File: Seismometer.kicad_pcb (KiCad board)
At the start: 4 copper layers, 91 parts, among them J4 Conn_01x03_Socket, J5 Conn_01x03_Socket, J6 Conn_01x03_Socket, U1 DLVR-F50D, U2 MC3479, U3 ADS131M04-Q1, U4 LP5907MFX-3.3, U5 Teensy4.1, X1 ASE-xxxMHz

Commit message: Initial layout complete
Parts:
- moved R22 55.8 mm to (156.7, 150.9)
- moved R1 43.9 mm to (131.5, 135.6), turned to 180 degrees
- moved R2 43.6 mm to (131.5, 133.1), turned to 180 degrees
- moved R48 29.5 mm to (175.3, 153.9)
- moved C12 29.5 mm to (175.3, 151.6)
- moved C14 29.5 mm to (180.8, 149.4)
- moved FB2 29.5 mm to (175.3, 149.4)
- moved U4 29.5 mm to (180.9, 153.0)
- moved R25 29.3 mm to (156.5, 115.3)
- moved R6 25.4 mm to (156.7, 105.2)
- moved C5 22.6 mm to (106.4, 116.9), turned to -90 degrees
- moved C6 22.2 mm to (108.5, 116.8), turned to -90 degrees
- moved R3 21.6 mm to (177.8, 135.9)
- moved R39 19.7 mm to (181.4, 135.9), turned to 0 degrees
- moved C1 18.8 mm to (166.8, 124.0)
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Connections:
- C3 pad 1: /3V3_TEENSY -> Net-(C3-Pad1)
- C4 pad 1: /3V3_TEENSY -> GND
- C4 pad 2: GND -> Net-(C4-Pad2)
- R21 pad 1: GND -> /~{CS_ACCEL}
- R22 pad 2: Net-(U5-32_OUT1B) -> Net-(U5-0_RX1_CRX2_CS1)
- R25 pad 1: Net-(U5-35_TX8) -> GND
- R25 pad 2: GND -> Net-(U5-24_A10_TX6_SCL2)
- R46 pad 2: Net-(U5-24_A10_TX6_SCL2) -> /ADC_DRDY
- R47 pad 2: Net-(U5-28_RX7) -> /ADC_SYNC/RESET
- R5 pad 2: /~{CS_ACCEL} -> /~{CS_ADC}
- R6 pad 1: Net-(U5-36_CS) -> GND
- R6 pad 2: /~{CS_ADC} -> Net-(U5-28_RX7)
- U5 pad 15: /3V3_TEENSY -> Net-(C4-Pad2)
- U5 pad 2: /INT_ACCEL -> Net-(U5-0_RX1_CRX2_CS1)
- U5 pad 24: Net-(U5-32_OUT1B) -> /INT_ACCEL
- U5 pad 27: Net-(U5-35_TX8) -> /ADC_DRDY
- U5 pad 28: Net-(U5-36_CS) -> /ADC_SYNC/RESET
- U5 pad 46: /3V3_TEENSY -> Net-(C3-Pad1)
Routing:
- net /SCK: track 0.00 -> 103.9 mm, vias 0 -> 3
- net /MOSI: track 0.00 -> 94.8 mm, vias 0 -> 2
- net /MISO: track 0.00 -> 86.1 mm, vias 0 -> 2
- net /SDA: track 0.00 -> 42.3 mm
- net /SCL: track 0.00 -> 42.3 mm
- net /Geophone Z/V-: track 2.24 -> 43.8 mm
- net Net-(U5-VIN): track 6.36 -> 47.5 mm
- net /Geophone Z/V+: track 2.35 -> 42.0 mm
- net /Geophone Y/V+: track 2.35 -> 38.4 mm
- net /INT_DLVR: track 1.80 -> 34.7 mm
- net /Geophone Y/V-: track 2.24 -> 31.4 mm
- net /INT_ACCEL: track 0.00 -> 21.9 mm
- net /ADC_DRDY: track 0.00 -> 21.3 mm
- net /~{CS_ADC}: track 0.00 -> 19.0 mm
- net /ADC_SYNC/RESET: track 0.00 -> 18.2 mm
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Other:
- board outline added: 92.7 x 65 mm

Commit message: Ready
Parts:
- added REF**: MountingHole_3.2mm_M3_DIN965, MountingHole:MountingHole_3.2mm_M3_DIN965, F.Cu at (119.6, 125.2)
- added REF**: MountingHole_3.2mm_M3_DIN965, MountingHole:MountingHole_3.2mm_M3_DIN965, F.Cu at (180.2, 79.8)
- added REF**: MountingHole_3.2mm_M3_DIN965, MountingHole:MountingHole_3.2mm_M3_DIN965, F.Cu at (97.5, 69.2)
- added REF**: MountingHole_3.2mm_M3_DIN965, MountingHole:MountingHole_3.2mm_M3_DIN965, F.Cu at (180.2, 115.6)
- X1: value ASE-xxxMHz -> SIT8924BA-22-33E-8.192000G
- moved C18 26.3 mm to (113.9, 123.6)
- moved R37 26.3 mm to (130.0, 117.0)
- moved R52 26.3 mm to (108.0, 103.5)
- moved R8 26.3 mm to (155.2, 117.0)
- moved C1 26.3 mm to (165.3, 97.7)
- moved C10 26.3 mm to (105.6, 76.7)
- moved C11 26.3 mm to (111.7, 72.9)
- moved C12 26.3 mm to (173.8, 125.3)
- moved C13 26.3 mm to (111.7, 68.8)
- moved C14 26.3 mm to (179.3, 123.1)
- moved C15 26.3 mm to (130.0, 127.2)
- moved C2 26.3 mm to (130.0, 124.9)
- moved C3 26.3 mm to (130.0, 122.1)
- moved C4 26.3 mm to (155.2, 91.6)
- moved C5 26.3 mm to (105.0, 90.7)
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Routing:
- net /MISO: track 86.1 -> 87.2 mm, vias 2 -> 0
- net GND: track 9.66 -> 10.0 mm, vias 68 -> 67
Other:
- board text added: "1 TOP"
- board text added: "2 GND"
- board text added: "3 PWR"
- board text added: "4 BOTTOM"
- board text added: "Seismometer V0.1"
- board text added: "Sytse Reitsma"

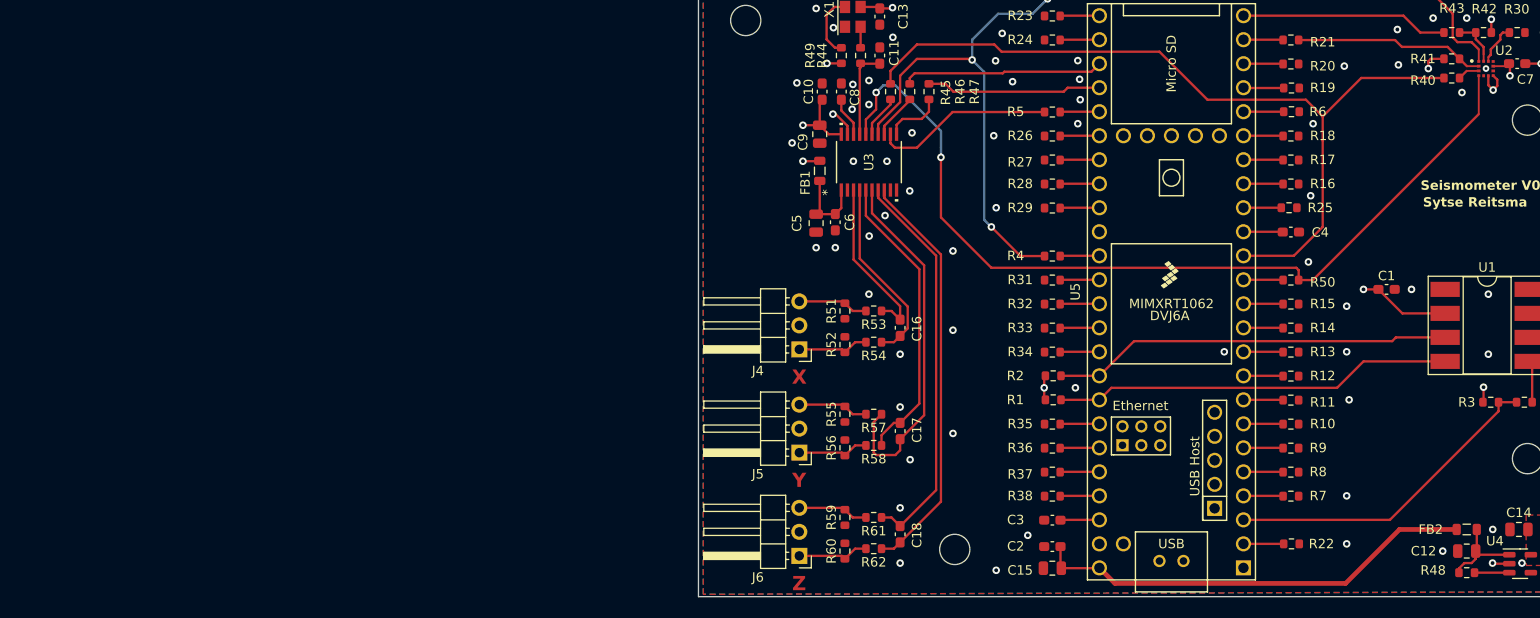
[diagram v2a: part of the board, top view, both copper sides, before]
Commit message: Active input filter
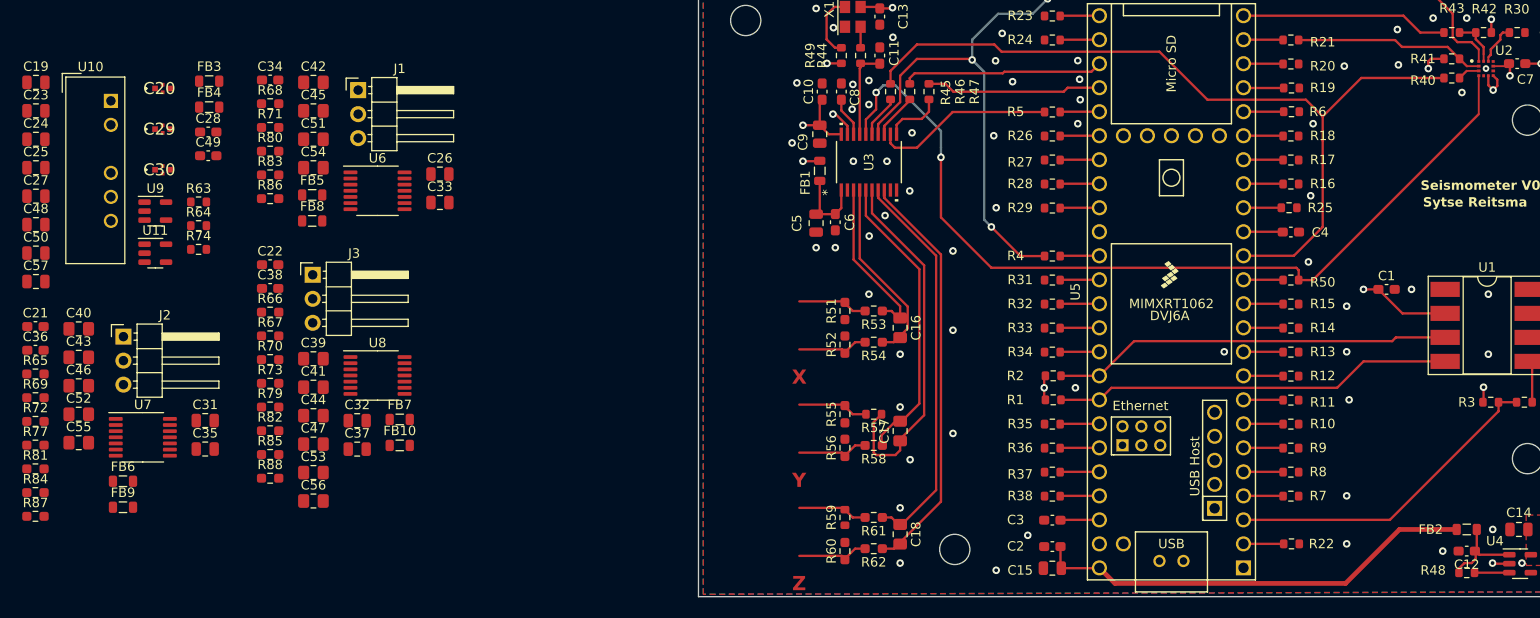
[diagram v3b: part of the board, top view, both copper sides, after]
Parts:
- removed J4, J5, J6: Conn_01x03_Socket, Connector_PinHeader_2.54mm:PinHeader_1x03_P2.54mm_Horizontal
- added C19: 2.2u, Capacitor_SMD:C_0805_2012Metric, F.Cu at (22.4, 75.8)
- added C20: NFM18PC104R1C3D, seismometer:NFM18PC104R1C3D, F.Cu at (35.8, 76.4)
- added C21: 100n, Capacitor_SMD:C_0603_1608Metric_Pad1.08x0.95mm_HandSolder, F.Cu at (22.4, 101.6)
- added C22: 100n, Capacitor_SMD:C_0603_1608Metric_Pad1.08x0.95mm_HandSolder, F.Cu at (47.2, 95.1)
- added C23: 100n, Capacitor_SMD:C_0805_2012Metric, F.Cu at (22.4, 78.8)
- added C24: 2.2u, Capacitor_SMD:C_0805_2012Metric, F.Cu at (22.4, 81.8)
- added C25: 2.2u, Capacitor_SMD:C_0805_2012Metric, F.Cu at (22.4, 84.8)
- added C26: 2.2u, Capacitor_SMD:C_0805_2012Metric, F.Cu at (65.2, 85.5)
- added C27: 2.2u, Capacitor_SMD:C_0805_2012Metric, F.Cu at (22.4, 87.8)
- added C28: 100n, Capacitor_SMD:C_0603_1608Metric_Pad1.08x0.95mm_HandSolder, F.Cu at (40.7, 81.0)
- added C29: NFM18PC104R1C3D, seismometer:NFM18PC104R1C3D, F.Cu at (35.8, 80.7)
- added C30: NFM18PC104R1C3D, seismometer:NFM18PC104R1C3D, F.Cu at (35.8, 85.0)
- added C31: 2.2u, Capacitor_SMD:C_0805_2012Metric, F.Cu at (40.3, 111.5)
- added C32: 2.2u, Capacitor_SMD:C_0805_2012Metric, F.Cu at (56.4, 111.6)
- added C33: 2.2u, Capacitor_SMD:C_0805_2012Metric, F.Cu at (65.2, 88.5)
- added C34: 100n, Capacitor_SMD:C_0603_1608Metric_Pad1.08x0.95mm_HandSolder, F.Cu at (47.2, 75.5)
- added C35: 2.2u, Capacitor_SMD:C_0805_2012Metric, F.Cu at (40.3, 114.6)
- added C36: 100n, Capacitor_SMD:C_0603_1608Metric_Pad1.08x0.95mm_HandSolder, F.Cu at (22.4, 104.1)
- added C37: 2.2u, Capacitor_SMD:C_0805_2012Metric, F.Cu at (56.4, 114.6)
- added C38: 100n, Capacitor_SMD:C_0603_1608Metric_Pad1.08x0.95mm_HandSolder, F.Cu at (47.2, 97.6)
- added C39: 1.6u X7R, Capacitor_SMD:C_0805_2012Metric_Pad1.18x1.45mm_HandSolder, F.Cu at (51.8, 105.0)
- added C40: 10u X7R, Capacitor_SMD:C_0805_2012Metric_Pad1.18x1.45mm_HandSolder, F.Cu at (27.0, 101.8)
- added C41: 10u X7R, Capacitor_SMD:C_0805_2012Metric_Pad1.18x1.45mm_HandSolder, F.Cu at (51.8, 108.0)
- added C42: 360n X7R, Capacitor_SMD:C_0805_2012Metric_Pad1.18x1.45mm_HandSolder, F.Cu at (51.8, 75.8)
- added C43: 360n X7R, Capacitor_SMD:C_0805_2012Metric_Pad1.18x1.45mm_HandSolder, F.Cu at (27.0, 104.9)
- added C44: 360n X7R, Capacitor_SMD:C_0805_2012Metric_Pad1.18x1.45mm_HandSolder, F.Cu at (51.8, 111.0)
- added C45: 1.6u X7R, Capacitor_SMD:C_0805_2012Metric_Pad1.18x1.45mm_HandSolder, F.Cu at (51.8, 78.8)
- added C46: 1.6u X7R, Capacitor_SMD:C_0805_2012Metric_Pad1.18x1.45mm_HandSolder, F.Cu at (27.0, 107.9)
- added C47: 1.6u X7R, Capacitor_SMD:C_0805_2012Metric_Pad1.18x1.45mm_HandSolder, F.Cu at (51.8, 114.0)
- added C48: 2.2u, Capacitor_SMD:C_0805_2012Metric, F.Cu at (22.4, 90.8)
- added C49: 100n, Capacitor_SMD:C_0603_1608Metric_Pad1.08x0.95mm_HandSolder, F.Cu at (40.7, 83.5)
- added C50: 1u, Capacitor_SMD:C_0805_2012Metric, F.Cu at (22.4, 93.8)
- added C51: 10u X7R, Capacitor_SMD:C_0805_2012Metric_Pad1.18x1.45mm_HandSolder, F.Cu at (51.8, 81.8)
- added C52: 10u X7R, Capacitor_SMD:C_0805_2012Metric_Pad1.18x1.45mm_HandSolder, F.Cu at (27.0, 110.9)
- added C53: 10u X7R, Capacitor_SMD:C_0805_2012Metric_Pad1.18x1.45mm_HandSolder, F.Cu at (51.8, 117.0)
- added C54: 10u X7R, Capacitor_SMD:C_0805_2012Metric_Pad1.18x1.45mm_HandSolder, F.Cu at (51.8, 84.8)
- added C55: 10u X7R, Capacitor_SMD:C_0805_2012Metric_Pad1.18x1.45mm_HandSolder, F.Cu at (27.0, 113.9)
- added C56: 10u X7R, Capacitor_SMD:C_0805_2012Metric_Pad1.18x1.45mm_HandSolder, F.Cu at (51.8, 120.1)
- added C57: 100n, Capacitor_SMD:C_0805_2012Metric, F.Cu at (22.4, 96.8)
- added FB10: MPZ1608S102ATA00, Inductor_SMD:L_0805_2012Metric, F.Cu at (60.9, 114.2)
- added FB3: MPZ1608S102ATA00, Inductor_SMD:L_0805_2012Metric, F.Cu at (40.8, 75.6)
- added FB4: MPZ1608S102ATA00, Inductor_SMD:L_0805_2012Metric, F.Cu at (40.8, 78.4)
- added FB5: MPZ1608S102ATA00, Inductor_SMD:L_0805_2012Metric, F.Cu at (51.7, 87.7)
- added FB6: MPZ1608S102ATA00, Inductor_SMD:L_0805_2012Metric, F.Cu at (31.6, 118.0)
- added FB7: MPZ1608S102ATA00, Inductor_SMD:L_0805_2012Metric, F.Cu at (60.9, 111.4)
- added FB8: MPZ1608S102ATA00, Inductor_SMD:L_0805_2012Metric, F.Cu at (51.7, 90.4)
- added FB9: MPZ1608S102ATA00, Inductor_SMD:L_0805_2012Metric, F.Cu at (31.6, 120.7)
- added J1: Conn_01x03_Socket, Connector_PinHeader_2.54mm:PinHeader_1x03_P2.54mm_Horizontal, F.Cu at (56.5, 76.6)
- added J2: Conn_01x03_Socket, Connector_PinHeader_2.54mm:PinHeader_1x03_P2.54mm_Horizontal, F.Cu at (31.7, 102.7)
- added J3: Conn_01x03_Socket, Connector_PinHeader_2.54mm:PinHeader_1x03_P2.54mm_Horizontal, F.Cu at (51.7, 96.1)
- added R63: 1.1, Resistor_SMD:R_0603_1608Metric, F.Cu at (39.6, 88.4)
- added R64: 10k, Resistor_SMD:R_0603_1608Metric, F.Cu at (39.6, 90.9)
- added R65: 9k TF, Resistor_SMD:R_0603_1608Metric_Pad0.98x0.95mm_HandSolder, F.Cu at (22.4, 106.6)
- added R66: 1k TF, Resistor_SMD:R_0603_1608Metric_Pad0.98x0.95mm_HandSolder, F.Cu at (47.2, 100.1)
- added R67: 9k TF, Resistor_SMD:R_0603_1608Metric_Pad0.98x0.95mm_HandSolder, F.Cu at (47.2, 102.6)
- added R68: 80.4k TF, Resistor_SMD:R_0603_1608Metric_Pad0.98x0.95mm_HandSolder, F.Cu at (47.2, 78.0)
- added R69: 80.4k TF, Resistor_SMD:R_0603_1608Metric_Pad0.98x0.95mm_HandSolder, F.Cu at (22.4, 109.1)
- added R70: 80.4k TF, Resistor_SMD:R_0603_1608Metric_Pad0.98x0.95mm_HandSolder, F.Cu at (47.2, 105.1)
- added R71: 1.5k TF, Resistor_SMD:R_0603_1608Metric_Pad0.98x0.95mm_HandSolder, F.Cu at (47.2, 80.5)
- added R72: 1.5k TF, Resistor_SMD:R_0603_1608Metric_Pad0.98x0.95mm_HandSolder, F.Cu at (22.4, 111.6)
- added R73: 1.5k TF, Resistor_SMD:R_0603_1608Metric_Pad0.98x0.95mm_HandSolder, F.Cu at (47.2, 107.6)
- added R74: 10k, Resistor_SMD:R_0603_1608Metric, F.Cu at (39.6, 93.4)
- added R77: 8.25k TF, Resistor_SMD:R_0603_1608Metric_Pad0.98x0.95mm_HandSolder, F.Cu at (22.4, 114.1)
- added R79: 8.25k TF, Resistor_SMD:R_0603_1608Metric_Pad0.98x0.95mm_HandSolder, F.Cu at (47.2, 110.1)
- added R80: 322k TF, Resistor_SMD:R_0603_1608Metric_Pad0.98x0.95mm_HandSolder, F.Cu at (47.2, 83.0)
- added R81: 322k TF, Resistor_SMD:R_0603_1608Metric_Pad0.98x0.95mm_HandSolder, F.Cu at (22.4, 116.7)
- added R82: 322k TF, Resistor_SMD:R_0603_1608Metric_Pad0.98x0.95mm_HandSolder, F.Cu at (47.2, 112.6)
- added R83: 15k TF, Resistor_SMD:R_0603_1608Metric_Pad0.98x0.95mm_HandSolder, F.Cu at (47.2, 85.6)
- added R84: 15k TF, Resistor_SMD:R_0603_1608Metric_Pad0.98x0.95mm_HandSolder, F.Cu at (22.4, 119.2)
- added R85: 15k TF, Resistor_SMD:R_0603_1608Metric_Pad0.98x0.95mm_HandSolder, F.Cu at (47.2, 115.1)
- added R86: 28.8k TF, Resistor_SMD:R_0603_1608Metric_Pad0.98x0.95mm_HandSolder, F.Cu at (47.2, 88.1)
- added R87: 28.8k TF, Resistor_SMD:R_0603_1608Metric_Pad0.98x0.95mm_HandSolder, F.Cu at (22.4, 121.7)
- added R88: 28.8k TF, Resistor_SMD:R_0603_1608Metric_Pad0.98x0.95mm_HandSolder, F.Cu at (47.2, 117.6)
- added U10: TBA1-0521E, Converter_DCDC:Converter_DCDC_TRACO_TBA1-xxxxE_Dual_THT, F.Cu at (30.4, 77.7)
- added U11: TPS72301DBV, Package_TO_SOT_SMD:SOT-23-5, F.Cu at (35.1, 93.8)
- added U6: OPA4387, Package_SO:TSSOP-14_4.4x5mm_P0.65mm, F.Cu at (58.6, 87.2)
- added U7: OPA4387, Package_SO:TSSOP-14_4.4x5mm_P0.65mm, F.Cu at (33.7, 113.3)
- added U8: OPA4387, Package_SO:TSSOP-14_4.4x5mm_P0.65mm, F.Cu at (58.6, 106.8)
- added U9: TPS7A2015PDBVR, Package_TO_SOT_SMD:SOT-23-5, F.Cu at (35.1, 89.4)
- C11: value 10p -> 12p
- C12: value 1u -> 100n; footprint Capacitor_SMD:C_0805_2012Metric -> Capacitor_SMD:C_0603_1608Metric_Pad1.08x0.95mm_HandSolder
- C15: value 1u -> 2.2u
- C16, C18: value 220n -> 1.6u X7R; footprint Capacitor_SMD:C_0603_1608Metric_Pad1.08x0.95mm_HandSolder -> Capacitor_SMD:C_0805_2012Metric_Pad1.18x1.45mm_HandSolder
- C17: value 220n -> 10u X7R; footprint Capacitor_SMD:C_0603_1608Metric_Pad1.08x0.95mm_HandSolder -> Capacitor_SMD:C_0805_2012Metric_Pad1.18x1.45mm_HandSolder
- R48: value 100k -> 10k
- R51, R52: value 100k -> 161k TF; footprint Resistor_SMD:R_0603_1608Metric -> Resistor_SMD:R_0603_1608Metric_Pad0.98x0.95mm_HandSolder
- R53: value 470 -> 161k TF; footprint Resistor_SMD:R_0603_1608Metric -> Resistor_SMD:R_0603_1608Metric_Pad0.98x0.95mm_HandSolder
- R54: value 470 -> 9.84k TF; footprint Resistor_SMD:R_0603_1608Metric -> Resistor_SMD:R_0603_1608Metric_Pad0.98x0.95mm_HandSolder
- R55, R56: value 100k -> 9.84k TF; footprint Resistor_SMD:R_0603_1608Metric -> Resistor_SMD:R_0603_1608Metric_Pad0.98x0.95mm_HandSolder
- R57: value 470 -> 22k 0.1%
- R58: value 470 -> 8.25k TF; footprint Resistor_SMD:R_0603_1608Metric -> Resistor_SMD:R_0603_1608Metric_Pad0.98x0.95mm_HandSolder
- R59: value 100k -> 82k 0.1%
- R60: value 100k -> 1k TF; footprint Resistor_SMD:R_0603_1608Metric -> Resistor_SMD:R_0603_1608Metric_Pad0.98x0.95mm_HandSolder
- R61: value 470 -> 9k TF; footprint Resistor_SMD:R_0603_1608Metric -> Resistor_SMD:R_0603_1608Metric_Pad0.98x0.95mm_HandSolder
- R62: value 470 -> 1k TF; footprint Resistor_SMD:R_0603_1608Metric -> Resistor_SMD:R_0603_1608Metric_Pad0.98x0.95mm_HandSolder
- U4: value LP5907MFX-3.3 -> TPS7A2033PDBVR
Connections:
- C12 pad 1: Net-(U4-IN) -> Net-(U11-EN)
- C15 pad 1: Net-(U5-VIN) -> Net-(C15-Pad1)
- C16 pad 1: /Geophone X/V+ -> Net-(U6A-+)
- C16 pad 2: /Geophone X/V- -> GND
- C17 pad 1: /Geophone Y/V+ -> Net-(U6C-+)
- C17 pad 2: /Geophone Y/V- -> Net-(C17-Pad2)
- C18 pad 1: /Geophone Z/V+ -> Net-(U7A-+)
- C18 pad 2: /Geophone Z/V- -> GND
- C2 pad 1: Net-(U5-VIN) -> GND
- C2 pad 2: GND -> Net-(U6E-V+)
- FB2 pad 1: Net-(U5-VIN) -> Net-(U10-+Vout)
- FB2 pad 2: Net-(U4-IN) -> Net-(C29-Pad1)
- R51 pad 2: Net-(J4-Pin_3) -> Net-(U6B-+)
- R52 pad 1: Net-(J4-Pin_1) -> GND
- R52 pad 2: GND -> Net-(U7B-+)
- R53 pad 1: /Geophone X/V+ -> GND
- R53 pad 2: Net-(J4-Pin_3) -> Net-(U8B-+)
- R54 pad 1: /Geophone X/V- -> Net-(U6A-+)
- R54 pad 2: Net-(J4-Pin_1) -> Net-(J1-Pin_2)
- R55 pad 1: GND -> Net-(U7A-+)
- R55 pad 2: Net-(J5-Pin_3) -> Net-(J2-Pin_2)
- R56 pad 1: Net-(J5-Pin_1) -> Net-(U8A-+)
- R56 pad 2: GND -> Net-(J3-Pin_2)
- R57 pad 1: /Geophone Y/V+ -> -1.5V
- R57 pad 2: Net-(J5-Pin_3) -> Net-(U11-FB)
- R58 pad 1: /Geophone Y/V- -> Net-(C51-Pad2)
- R58 pad 2: Net-(J5-Pin_1) -> Net-(U6B--)
- R59 pad 1: GND -> Net-(U11-FB)
- R59 pad 2: Net-(J6-Pin_3) -> GND
- R60 pad 1: Net-(J6-Pin_1) -> GND
- R60 pad 2: GND -> Net-(U6A--)
- R61 pad 1: /Geophone Z/V+ -> Net-(C54-Pad1)
- R61 pad 2: Net-(J6-Pin_3) -> Net-(U6A--)
- R62 pad 1: /Geophone Z/V- -> GND
- R62 pad 2: Net-(J6-Pin_1) -> Net-(U7A--)
- U3 pad 4: /Geophone X/V- -> GND
- U3 pad 5: /Geophone Y/V- -> GND
- U3 pad 8: /Geophone Z/V- -> GND
- U5 pad 48: Net-(U5-VIN) -> /Power/VUSB
- U5 pad 49: unconnected-(U5-VUSB-Pad49) -> /Power/VUSB
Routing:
- net GND: track 10.0 -> 101.0 mm
- net Net-(U5-VIN): track 47.2 -> 0.00 mm
- net /Geophone Z/V-: track 43.8 -> 0.00 mm

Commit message: wip Layout
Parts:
- removed R10, R11, R12, R13, R14, R15, R16, R17, R18, R19, R20, R22, R23, R24, R25, R26, R27, R28, R29, R31, R32, R33, R34, R35, R36, R37, R38, R47, R7, R8, R9: 51, Resistor_SMD:R_0603_1608Metric
- added C58: 2.2u, Capacitor_SMD:C_1206_3216Metric, F.Cu at (205.2, 79.7)
- added C59: 2.2u, Capacitor_SMD:C_1206_3216Metric, F.Cu at (198.5, 79.7)
- added C60: 2.2u, Capacitor_SMD:C_1206_3216Metric, F.Cu at (205.2, 85.9)
- added C61: 2.2u, Capacitor_SMD:C_1206_3216Metric, F.Cu at (198.5, 85.9)
- added R75: 1.1, Resistor_SMD:R_0603_1608Metric, F.Cu at (202.0, 79.7)
- added R76: 1.1, Resistor_SMD:R_0603_1608Metric, F.Cu at (202.0, 85.9)
- C14, C15, C19, C24, C25, C26, C27, C31, C32, C33, C35, C37, C48, C5, C50, C9: footprint Capacitor_SMD:C_0805_2012Metric -> Capacitor_SMD:C_1206_3216Metric
- C16, C17, C18, C39, C40, C41, C45, C46, C47, C51, C52, C53, C54, C55, C56: footprint Capacitor_SMD:C_0805_2012Metric_Pad1.18x1.45mm_HandSolder -> Capacitor_SMD:C_1206_3216Metric
- moved C23 185.5 mm to (203.9, 117.0)
- moved C24 184.3 mm to (203.9, 113.7)
- moved C50 182.5 mm to (204.7, 102.6)
- moved C57 182.0 mm to (204.2, 106.0)
- moved C19 176.1 mm to (198.5, 73.5), turned to -90 degrees
- moved C27 175.7 mm to (198.0, 94.0), turned to 180 degrees
- moved C25 172.9 mm to (192.6, 115.8), turned to 180 degrees
- moved C48 172.5 mm to (194.5, 102.9), turned to 180 degrees
- moved C20 166.3 mm to (201.9, 68.6), turned to -90 degrees
- moved U9 165.2 mm to (199.5, 104.8)
- moved U11 164.8 mm to (198.2, 116.7)
- moved R63 163.1 mm to (202.1, 73.5), turned to -90 degrees
- moved C29 162.9 mm to (198.4, 91.4)
- moved U10 162.4 mm to (192.7, 70.9)
- moved C30 159.7 mm to (192.9, 113.5)
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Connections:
- net Net-(U10-+Vout) renamed +5V
- net Net-(U10--Vout) renamed -5V
- C17 pad 1: Net-(U6C-+) -> Net-(C17-Pad1)
- C17 pad 2: Net-(C17-Pad2) -> Net-(U6C-+)
- C20 pad A2: (no net) -> GND
- C20 pad B2: (no net) -> GND
- C29 pad A2: (no net) -> GND
- C29 pad B2: (no net) -> GND
- C30 pad A2: (no net) -> GND
- C30 pad B2: (no net) -> GND
- C40 pad 1: Net-(U7C-+) -> Net-(C40-Pad1)
- C40 pad 2: Net-(C40-Pad2) -> Net-(U7C-+)
- C41 pad 1: Net-(U8C-+) -> Net-(C41-Pad1)
- C41 pad 2: Net-(C41-Pad2) -> Net-(U8C-+)
- C51 pad 1: Net-(C17-Pad2) -> Net-(C17-Pad1)
- C52 pad 1: Net-(C40-Pad2) -> Net-(C40-Pad1)
- C53 pad 1: Net-(C41-Pad2) -> Net-(C41-Pad1)
- J1 pad 3: (no net) -> GND
- J2 pad 3: (no net) -> GND
- J3 pad 3: (no net) -> GND
- R6 pad 1: GND -> Net-(U5-36_CS)
- R6 pad 2: Net-(U5-28_RX7) -> /ADC_SYNC/RESET
- R68 pad 2: Net-(C17-Pad2) -> Net-(C17-Pad1)
- R69 pad 2: Net-(C40-Pad2) -> Net-(C40-Pad1)
- R70 pad 2: Net-(C41-Pad2) -> Net-(C41-Pad1)
- U3 pad 11: Net-(U3-SYNC/RESET) -> /ADC_SYNC/RESET
- U5 pad 10: Net-(U5-8_TX2_IN1) -> unconnected-(U5-8_TX2_IN1-Pad10)
- U5 pad 11: Net-(U5-9_OUT1C) -> unconnected-(U5-9_OUT1C-Pad11)
- U5 pad 12: Net-(U5-10_CS_MQSR) -> unconnected-(U5-10_CS_MQSR-Pad12)
- U5 pad 16: Net-(U5-24_A10_TX6_SCL2) -> unconnected-(U5-24_A10_TX6_SCL2-Pad16)
- U5 pad 17: Net-(U5-25_A11_RX6_SDA2) -> unconnected-(U5-25_A11_RX6_SDA2-Pad17)
- U5 pad 18: Net-(U5-26_A12_MOSI1) -> unconnected-(U5-26_A12_MOSI1-Pad18)
- U5 pad 19: Net-(U5-27_A13_SCK1) -> unconnected-(U5-27_A13_SCK1-Pad19)
- U5 pad 2: Net-(U5-0_RX1_CRX2_CS1) -> unconnected-(U5-0_RX1_CRX2_CS1-Pad2)
- U5 pad 20: Net-(U5-28_RX7) -> unconnected-(U5-28_RX7-Pad20)
- U5 pad 21: Net-(U5-29_TX7) -> unconnected-(U5-29_TX7-Pad21)
- U5 pad 22: Net-(U5-30_CRX3) -> unconnected-(U5-30_CRX3-Pad22)
- U5 pad 25: Net-(U5-33_MCLK2) -> unconnected-(U5-33_MCLK2-Pad25)
- U5 pad 26: Net-(U5-34_RX8) -> unconnected-(U5-34_RX8-Pad26)
- U5 pad 28: /ADC_SYNC/RESET -> Net-(U5-36_CS)
- U5 pad 30: Net-(U5-38_CS1_IN1) -> unconnected-(U5-38_CS1_IN1-Pad30)
- U5 pad 31: Net-(U5-39_MISO1_OUT1A) -> unconnected-(U5-39_MISO1_OUT1A-Pad31)
- U5 pad 32: Net-(U5-40_A16) -> unconnected-(U5-40_A16-Pad32)
- U5 pad 33: Net-(U5-41_A17) -> unconnected-(U5-41_A17-Pad33)
- U5 pad 36: Net-(U5-14_A0_TX3_SPDIF_OUT) -> unconnected-(U5-14_A0_TX3_SPDIF_OUT-Pad36)
- U5 pad 37: Net-(U5-15_A1_RX3_SPDIF_IN) -> unconnected-(U5-15_A1_RX3_SPDIF_IN-Pad37)
- U5 pad 38: Net-(U5-16_A2_RX4_SCL1) -> unconnected-(U5-16_A2_RX4_SCL1-Pad38)
- U5 pad 39: Net-(U5-17_A3_TX4_SDA1) -> unconnected-(U5-17_A3_TX4_SDA1-Pad39)
- U5 pad 4: Net-(U5-2_OUT2) -> unconnected-(U5-2_OUT2-Pad4)
- U5 pad 42: Net-(U5-20_A6_TX5_LRCLK1) -> unconnected-(U5-20_A6_TX5_LRCLK1-Pad42)
- U5 pad 43: Net-(U5-21_A7_RX5_BCLK1) -> unconnected-(U5-21_A7_RX5_BCLK1-Pad43)
- U5 pad 44: Net-(U5-22_A8_CTX1) -> unconnected-(U5-22_A8_CTX1-Pad44)
- U5 pad 45: Net-(U5-23_A9_CRX1_MCLK1) -> unconnected-(U5-23_A9_CRX1_MCLK1-Pad45)
- U5 pad 5: Net-(U5-3_LRCLK2) -> unconnected-(U5-3_LRCLK2-Pad5)
- U5 pad 52: unconnected-(U5-GND-Pad52) -> GND
- U5 pad 6: Net-(U5-4_BCLK2) -> unconnected-(U5-4_BCLK2-Pad6)
- U5 pad 7: Net-(U5-5_IN2) -> unconnected-(U5-5_IN2-Pad7)
- U5 pad 8: Net-(U5-6_OUT1D) -> unconnected-(U5-6_OUT1D-Pad8)
- U5 pad 9: Net-(U5-7_RX2_OUT1A) -> unconnected-(U5-7_RX2_OUT1A-Pad9)
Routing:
- net GND: track 101.0 -> 16.9 mm, vias 67 -> 101
- net /SCK: track 103.9 -> 22.5 mm, vias 3 -> 0
- net /MISO: track 87.2 -> 13.5 mm
- net /MOSI: track 94.8 -> 30.7 mm
- net /SDA: track 42.3 -> 4.06 mm
- net /SCL: track 42.3 -> 4.06 mm
- net /INT_DLVR: track 34.7 -> 0.00 mm
- net /Geophone Y/V-: track 31.4 -> 0.00 mm
- net /Geophone Z/V+: track 42.0 -> 11.5 mm
- net /Geophone Y/V+: track 38.4 -> 11.5 mm
- net (no net): track 0.00 -> 25.0 mm
- net Net-(C47-Pad1): track 0.00 -> 23.1 mm, vias 0 -> 2
- net Net-(C45-Pad1): track 0.00 -> 23.1 mm, vias 0 -> 2
- net Net-(C46-Pad1): track 0.00 -> 23.1 mm, vias 0 -> 2
- net /INT_ACCEL: track 21.9 -> 0.00 mm
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- added copper zone on F.Cu, net +1V5
- added copper zone on F.Cu, net +5V
- added copper zone on F.Cu, net -1.5V
- added copper zone on F.Cu, net -5V
- added copper zone on F.Cu, net Net-(U10-+Vin)
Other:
- board size 92.7 x 65 mm -> 116.2 x 65 mm
- board text removed: "X"
- board text removed: "Y"
- board text removed: "Z"

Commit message: Layout done. Tweaking...
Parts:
- removed R21: 51, Resistor_SMD:R_0603_1608Metric
- added C62: 1u, Capacitor_SMD:C_1206_3216Metric, F.Cu at (146.6, 94.4)
- added R7: 51, Resistor_SMD:R_0603_1608Metric, F.Cu at (164.5, 111.1)
- U5: footprint seismometer:Teensy41 -> seismometer:Teensy41_minimal
- moved C1 101.2 mm to (146.6, 91.7)
- moved R6 81.5 mm to (164.5, 98.6)
- moved R1 77.1 mm to (141.9, 105.7)
- moved R2 77.1 mm to (141.9, 103.1)
- moved R5 57.9 mm to (164.5, 101.0)
- moved C20 57.5 mm to (193.3, 125.4), turned to 90 degrees
- moved FB4 57.1 mm to (196.8, 125.6), turned to 90 degrees
- moved R50 55.6 mm to (188.3, 95.9)
- moved C4 55.5 mm to (188.5, 90.8)
- moved C3 54.3 mm to (164.5, 121.3)
- moved R4 54.3 mm to (164.5, 93.3)
- moved U10 53.2 mm to (202.6, 123.2), turned to 180 degrees
- moved C15 49.6 mm to (190.0, 120.6), turned to 90 degrees
- moved R63 47.9 mm to (193.2, 120.5), turned to 90 degrees
- moved C19 47.0 mm to (196.7, 120.5), turned to 90 degrees
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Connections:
- R5 pad 1: Net-(U5-37_CS) -> Net-(U5-16_A2_RX4_SCL1)
- R6 pad 1: Net-(U5-36_CS) -> Net-(U5-15_A1_RX3_SPDIF_IN)
- U5 pad 23: Net-(U5-31_CTX3) -> unconnected-(U5-31_CTX3-Pad23)
- U5 pad 24: /INT_ACCEL -> unconnected-(U5-32_OUT1B-Pad24)
- U5 pad 27: /ADC_DRDY -> unconnected-(U5-35_TX8-Pad27)
- U5 pad 28: Net-(U5-36_CS) -> unconnected-(U5-36_CS-Pad28)
- U5 pad 29: Net-(U5-37_CS) -> unconnected-(U5-37_CS-Pad29)
- U5 pad 3: /INT_DLVR -> unconnected-(U5-1_TX1_CTX2_MISO1-Pad3)
- U5 pad 36: unconnected-(U5-14_A0_TX3_SPDIF_OUT-Pad36) -> /ADC_DRDY
- U5 pad 37: unconnected-(U5-15_A1_RX3_SPDIF_IN-Pad37) -> Net-(U5-15_A1_RX3_SPDIF_IN)
- U5 pad 38: unconnected-(U5-16_A2_RX4_SCL1-Pad38) -> Net-(U5-16_A2_RX4_SCL1)
- U5 pad 39: unconnected-(U5-17_A3_TX4_SDA1-Pad39) -> /INT_DLVR
- U5 pad 42: unconnected-(U5-20_A6_TX5_LRCLK1-Pad42) -> Net-(U5-20_A6_TX5_LRCLK1)
- U5 pad 43: unconnected-(U5-21_A7_RX5_BCLK1-Pad43) -> /INT_ACCEL
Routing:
- net /MOSI: track 30.7 -> 94.8 mm, vias 2 -> 0
- net /MISO: track 13.5 -> 65.5 mm, vias 0 -> 2
- net -5V: track 0.00 -> 49.8 mm, vias 0 -> 4
- net /Geophone Z/V+: track 11.5 -> 54.9 mm, vias 0 -> 2
- net /SCK: track 22.5 -> 59.2 mm, vias 0 -> 2
- net +5V: track 0.00 -> 26.4 mm
- net /SDA: track 4.06 -> 29.9 mm
- net +3V3: track 26.8 -> 52.1 mm, vias 10 -> 26
- net (no net): track 25.0 -> 0.00 mm
- net /Geophone Y/V+: track 11.5 -> 35.5 mm, vias 0 -> 2
- net /SCL: track 4.06 -> 27.7 mm
- net /~{CS_ADC}: track 9.30 -> 30.7 mm
- net /Geophone X/V+: track 11.5 -> 29.7 mm, vias 0 -> 2
- net /ADC_SYNC/RESET: track 10.5 -> 26.5 mm
- net /INT_ACCEL: track 0.00 -> 15.4 mm
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- added copper zone on In2.Cu, net +1V5
- added copper zone on B.Cu, net +3V3
- added copper zone on In2.Cu, net -1.5V
- added copper zone on F.Cu, net /Power/VUSB
